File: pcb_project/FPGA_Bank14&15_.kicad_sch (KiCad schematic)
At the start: 17 parts, among them IC3 IS61WV204816BLL-10TLI, U7 XC7A100T-FTG256, U8 MT25QL128ABA1ESE-0SIT

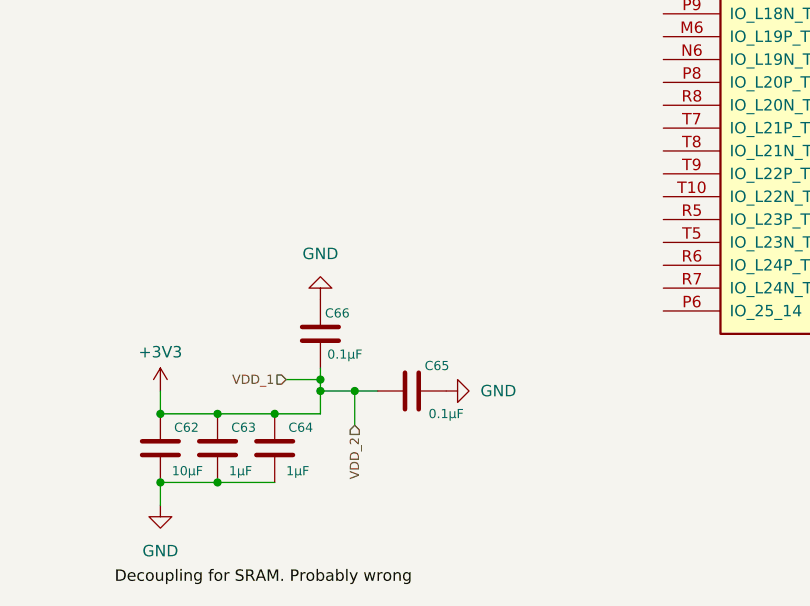
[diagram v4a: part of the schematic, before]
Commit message: 16bit binary weighted dac, FPGA power
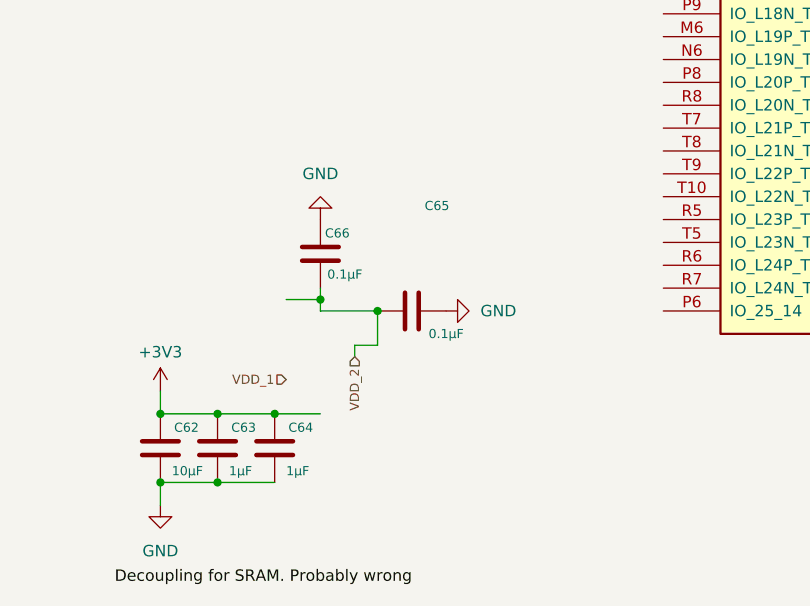
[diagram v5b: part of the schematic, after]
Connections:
- net +3V3: no longer C65.1, C66.2, IC3.12 (VDD_1), IC3.36 (VDD_2)
- new net VDD_1: IC3.12 (VDD_1)
- new net VDD_2: C65.1, C66.2, IC3.36 (VDD_2)
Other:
- moved on the sheet: C65, C66
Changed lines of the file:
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@@
 	(paper "A4")
 	(junction
+		(at 67.31 160.02)
+		(diameter 0)
+		(color 0 0 0 0)
+	)
+	(junction
 		(at 81.28 111.76)
 		(diameter 0)
@@
 	)
 	(junction
-		(at 60.96 167.64)
+		(at 60.96 158.75)
 		(diameter 0)
 		(color 0 0 0 0)
@@
 	)
 	(junction
-		(at 64.77 168.91)
-		(diameter 0)
-		(color 0 0 0 0)
-	)
-	(junction
 		(at 152.4 15.24)
 		(diameter 0)
@@
 	)
 	(junction
-		(at 60.96 168.91)
-		(diameter 0)
-		(color 0 0 0 0)
-	)
-	(junction
 		(at 262.89 74.93)
 		(diameter 0)
@@
 	(wire
 		(pts
-			(xy 64.77 168.91) (xy 67.31 168.91)
-		)
-		(stroke
-			(width 0)
-			(type default)
-		)
-	)
-	(wire
-		(pts
 			(xy 255.27 107.95) (xy 255.27 129.54)
 		)
@@
 	(wire
 		(pts
-			(xy 60.96 166.37) (xy 60.96 167.64)
+			(xy 60.96 157.48) (xy 60.96 158.75)
 		)
 		(stroke
@@
 	(wire
 		(pts
-			(xy 60.96 168.91) (xy 60.96 171.45)
-		)
-		(stroke
-			(width 0)
-			(type default)
-		)
-	)
-	(wire
-		(pts
-			(xy 64.77 168.91) (xy 64.77 172.72)
+			(xy 64.77 163.83) (xy 64.77 165.1)
 		)
 		(stroke
@@
 	(wire
 		(pts
-			(xy 57.15 167.64) (xy 60.96 167.64)
+			(xy 57.15 158.75) (xy 60.96 158.75)
 		)
 		(stroke
@@
 	(wire
 		(pts
+			(xy 64.77 163.83) (xy 67.31 163.83)
+		)
+		(stroke
+			(width 0)
+			(type default)
+		)
+	)
+	(wire
+		(pts
 			(xy 17.78 45.72) (xy 17.78 90.17)
 		)
@@
 	(wire
 		(pts
-			(xy 60.96 168.91) (xy 64.77 168.91)
+			(xy 60.96 160.02) (xy 67.31 160.02)
 		)
 		(stroke
@@
 	(wire
 		(pts
-			(xy 60.96 167.64) (xy 60.96 168.91)
+			(xy 60.96 158.75) (xy 60.96 160.02)
 		)
 		(stroke
@@
 	(wire
 		(pts
+			(xy 67.31 163.83) (xy 67.31 160.02)
+		)
+		(stroke
+			(width 0)
+			(type default)
+		)
+	)
+	(wire
+		(pts
 			(xy 204.47 85.09) (xy 204.47 106.68)
 		)
@@
 	(hierarchical_label "VDD_2"
 		(shape input)
-		(at 64.77 172.72 270)
+		(at 64.77 165.1 270)
 		(effects
 			(font
@@
 	(symbol
 		(lib_id "Device:C")
-		(at 71.12 168.91 90)
+		(at 71.12 160.02 90)
 		(unit 1)
 		(exclude_from_sim no)
@@
 		(dnp no)
 		(property "Reference" "C65"
-			(at 73.914 166.116 90)
+			(at 73.914 148.336 90)
 			(effects
 				(font
@@
 		)
 		(property "Value" "0.1µF"
-			(at 74.93 171.45 90)
+			(at 74.93 162.56 90)
 			(effects
 				(font
@@
 		)
 		(property "Footprint" ""
-			(at 74.93 167.9448 0)
+			(at 74.93 159.0548 0)
 			(effects
 				(font
@@
 		)
 		(property "Datasheet" "~"
-			(at 71.12 168.91 0)
+			(at 71.12 160.02 0)
 			(effects
 				(font
@@
 		)
 		(property "Description" "Unpolarized capacitor"
-			(at 71.12 168.91 0)
+			(at 71.12 160.02 0)
 			(effects
 				(font
@@
 	(symbol
 		(lib_id "Device:C")
-		(at 60.96 162.56 0)
+		(at 60.96 153.67 0)
 		(unit 1)
 		(exclude_from_sim no)
@@
 		(dnp no)
 		(property "Reference" "C66"
-			(at 61.468 160.274 0)
+			(at 61.468 151.384 0)
 			(effects
 				(font
@@
 		)
 		(property "Value" "0.1µF"
-			(at 61.722 164.846 0)
+			(at 61.722 155.956 0)
 			(effects
 				(font
@@
 		)
 		(property "Footprint" ""
-			(at 61.9252 166.37 0)
+			(at 61.9252 157.48 0)
 			(effects
 				(font
@@
 		)
 		(property "Datasheet" "~"
-			(at 60.96 162.56 0)
+			(at 60.96 153.67 0)
 			(effects
 				(font
@@
 		)
 		(property "Description" "Unpolarized capacitor"
-			(at 60.96 162.56 0)
+			(at 60.96 153.67 0)
 			(effects
 				(font
@@
 	(symbol
 		(lib_id "power:GND")
-		(at 74.93 168.91 90)
+		(at 74.93 160.02 90)
 		(unit 1)
 		(exclude_from_sim no)
@@
 		(fields_autoplaced yes)
 		(property "Reference" "#PWR066"
-			(at 81.28 168.91 0)
+			(at 81.28 160.02 0)
 			(effects
 				(font
@@
 		)
 		(property "Value" "GND"
-			(at 78.74 168.9099 90)
+			(at 78.74 160.0199 90)
 			(effects
 				(font
@@
 		)
 		(property "Footprint" ""
-			(at 74.93 168.91 0)
+			(at 74.93 160.02 0)
 			(effects
 				(font
@@
 		)
 		(property "Datasheet" ""
-			(at 74.93 168.91 0)
+			(at 74.93 160.02 0)
 			(effects
 				(font
@@
 		)
 		(property "Description" "Power symbol creates a global label with name \"GND\" , ground"
-			(at 74.93 168.91 0)
+			(at 74.93 160.02 0)
 			(effects
 				(font
@@
 	(symbol
 		(lib_id "power:GND")
-		(at 60.96 158.75 180)
+		(at 60.96 149.86 180)
 		(unit 1)
 		(exclude_from_sim no)
@@
 		(fields_autoplaced yes)
 		(property "Reference" "#PWR065"
-			(at 60.96 152.4 0)
+			(at 60.96 143.51 0)
 			(effects
 				(font
@@
 		)
 		(property "Value" "GND"
-			(at 60.96 153.67 0)
+			(at 60.96 144.78 0)
 			(effects
 				(font
@@
 		)
 		(property "Footprint" ""
-			(at 60.96 158.75 0)
+			(at 60.96 149.86 0)
 			(effects
 				(font
@@
 		)
 		(property "Datasheet" ""
-			(at 60.96 158.75 0)
+			(at 60.96 149.86 0)
 			(effects
 				(font
@@
 		)
 		(property "Description" "Power symbol creates a global label with name \"GND\" , ground"
-			(at 60.96 158.75 0)
+			(at 60.96 149.86 0)
 			(effects
 				(font

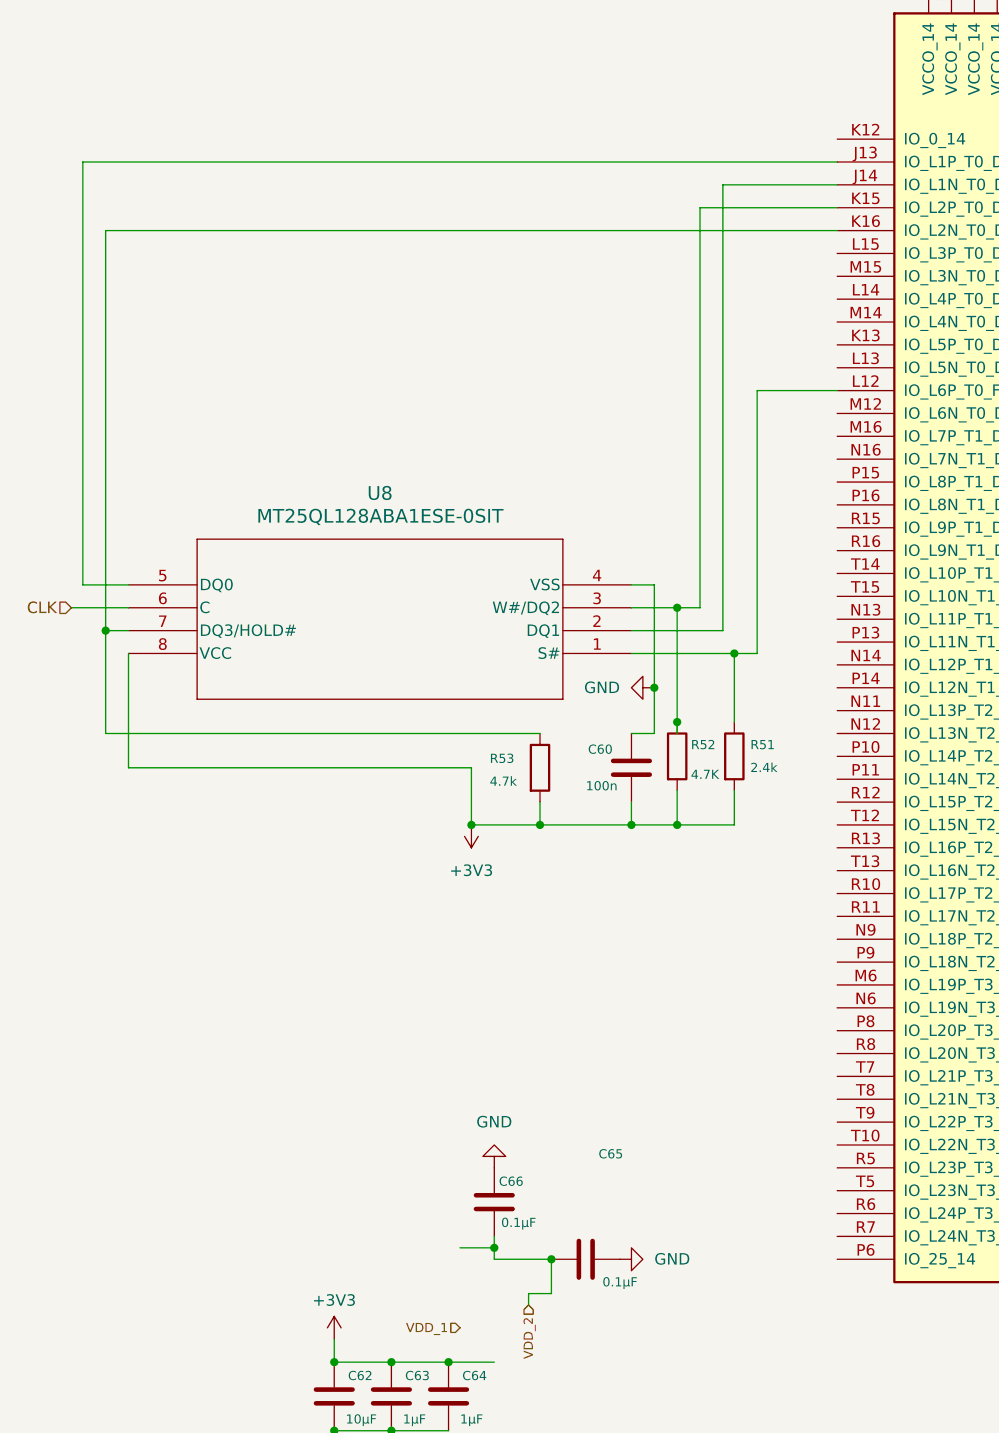
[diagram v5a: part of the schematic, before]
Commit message: Add pin placement for OSPI on FPGA, not wired in root yet
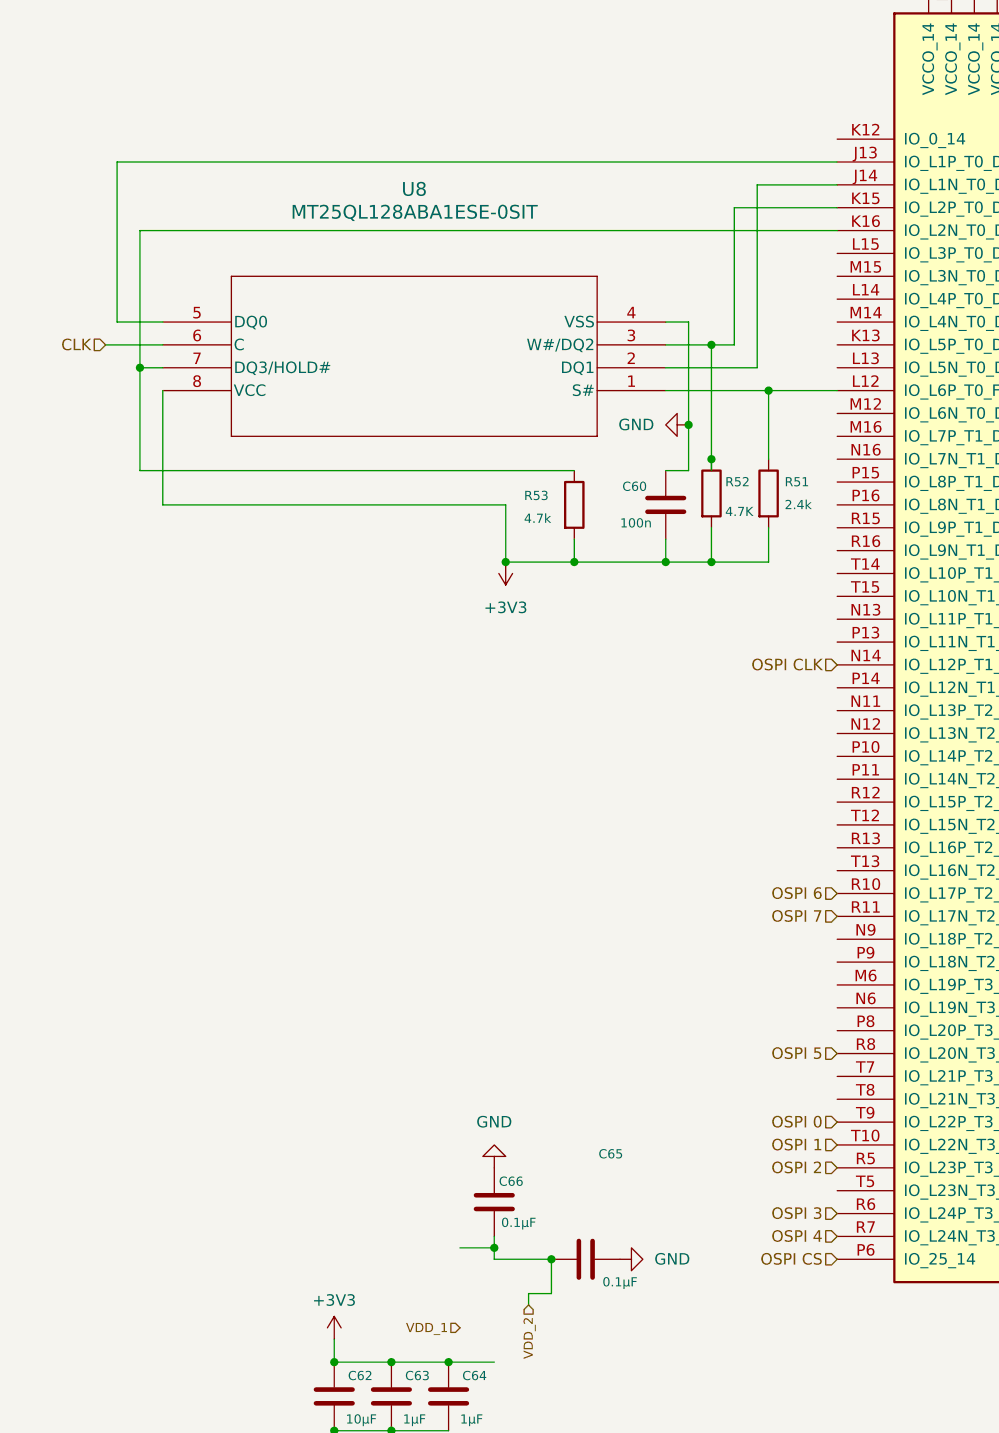
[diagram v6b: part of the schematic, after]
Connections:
- net OSPI CLK: now reaches U7.N14 (IO_L12P_T1_MRCC_14)
- net OSPI CS: now reaches U7.P6 (IO_25_14)
- net OSPI 6: now reaches U7.R10 (IO_L17P_T2_A14_D30_14)
- net OSPI 7: now reaches U7.R11 (IO_L17N_T2_A13_D29_14)
- net OSPI 2: now reaches U7.R5 (IO_L23P_T3_A03_D19_14)
- net OSPI 3: now reaches U7.R6 (IO_L24P_T3_A01_D17_14)
- net OSPI 4: now reaches U7.R7 (IO_L24N_T3_A00_D16_14)
- net OSPI 5: now reaches U7.R8 (IO_L20N_T3_A07_D23_14)
- net OSPI 1: now reaches U7.T10 (IO_L22N_T3_A04_D20_14)
- net OSPI 0: now reaches U7.T9 (IO_L22P_T3_A05_D21_14)
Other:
- moved on the sheet: C60, R51, R52, R53, U8

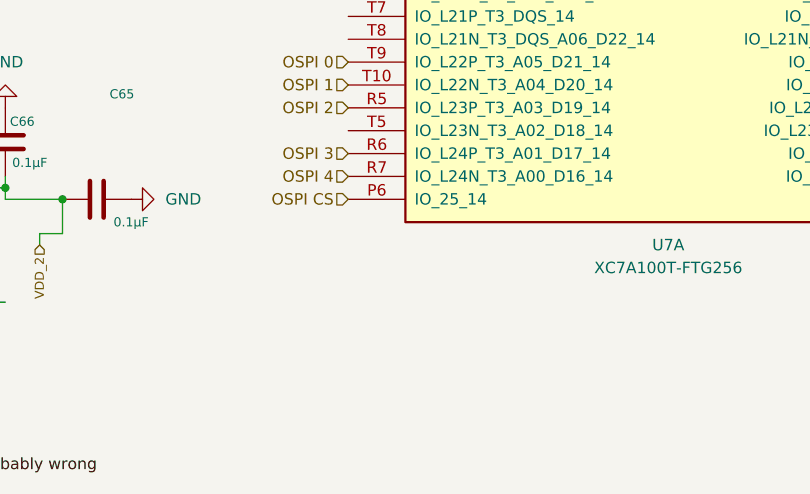
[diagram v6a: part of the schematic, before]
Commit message: SPI connection root
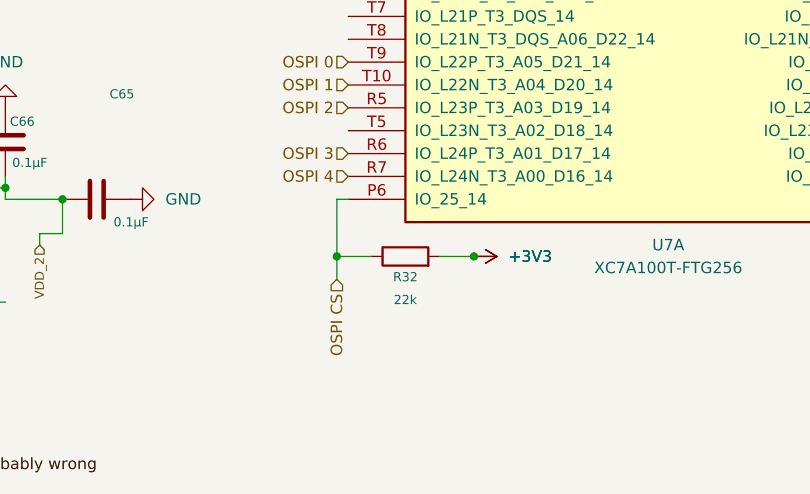
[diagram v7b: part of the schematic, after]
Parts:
- added R32: 22k, symbol Device:R
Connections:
- net +3V3: now also R32.2
- net OSPI CS: now also R32.1
